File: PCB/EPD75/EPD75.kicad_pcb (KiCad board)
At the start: 2 copper layers, 168 x 110 mm, 73 parts, among them J1 Conn_01x26, J2 Shelly, J3 USB-PROG, J4 BTN1, J5 USB-C-Socket-V, J6 BTN2, J7 USB-C-Socket-V, J8 PWR, P1 2, P10 +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

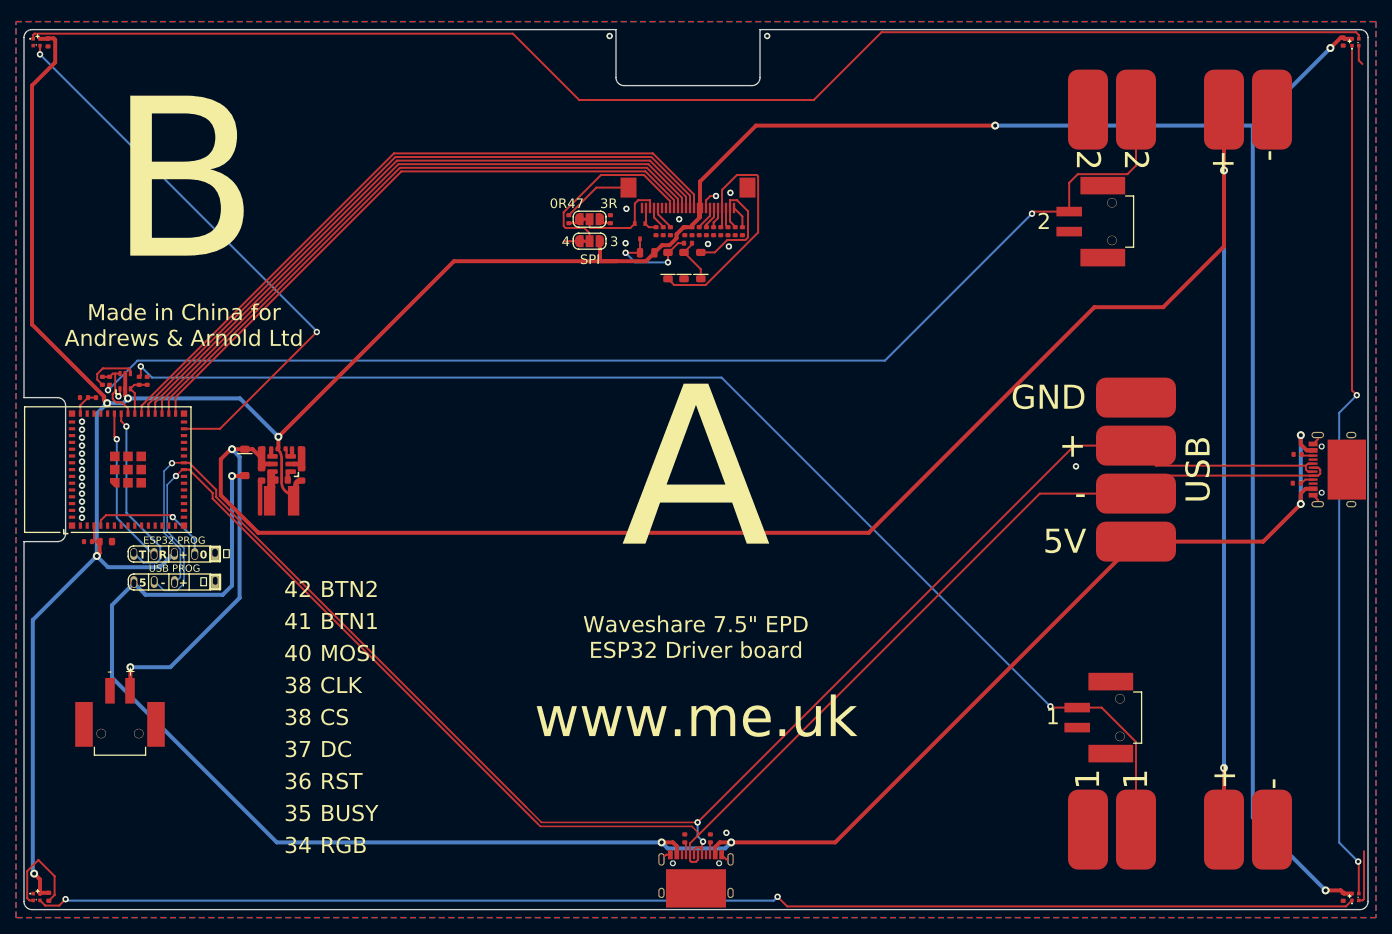
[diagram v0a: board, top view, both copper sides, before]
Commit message: Silk tweak
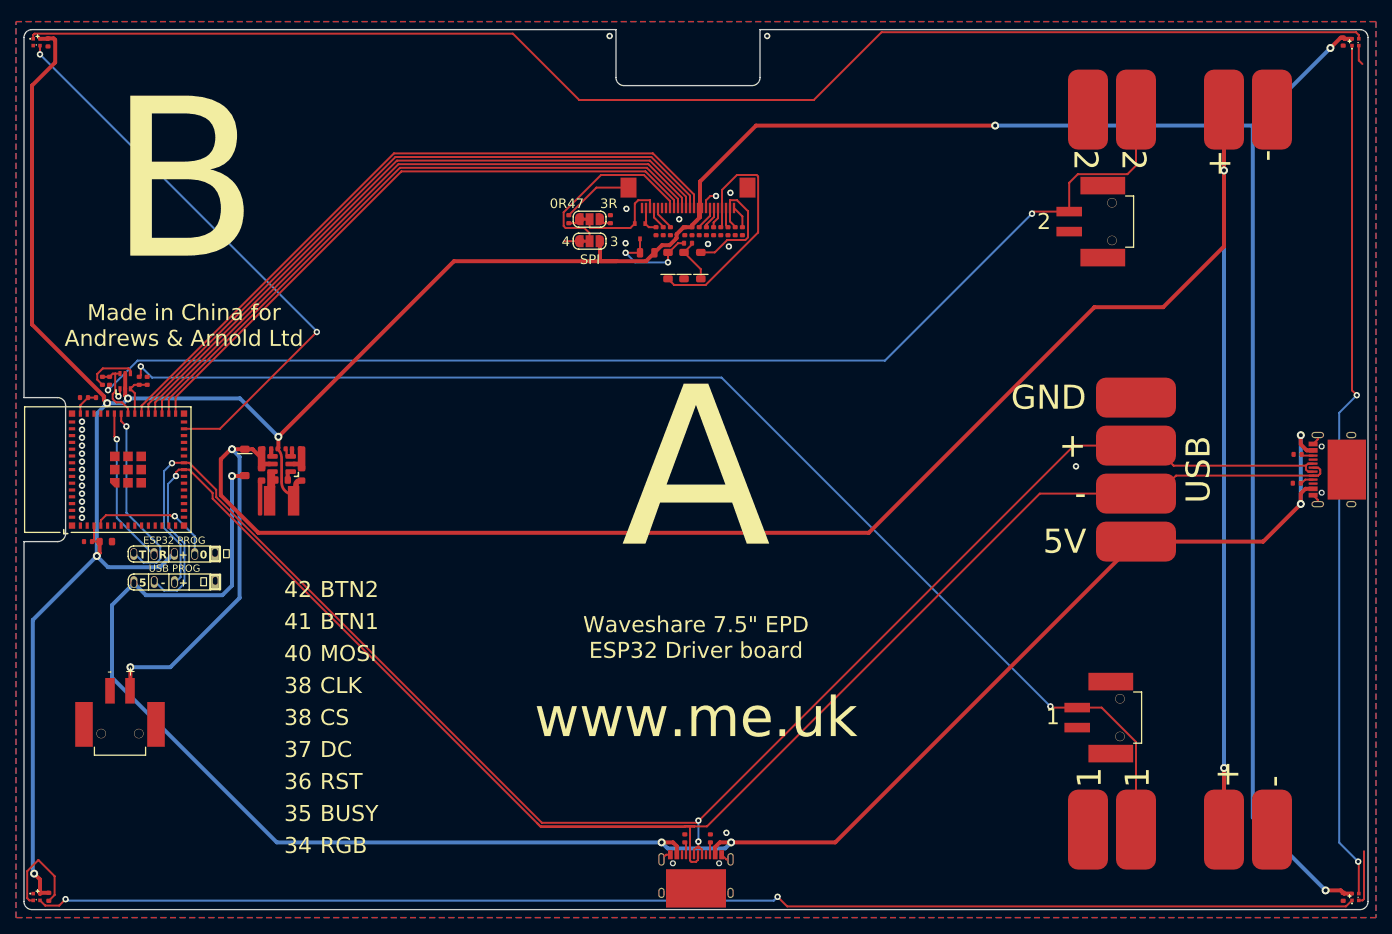
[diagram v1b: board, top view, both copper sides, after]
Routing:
- net D-: track 204.6 -> 224.8 mm
- net D+: track 207.4 -> 204.3 mm

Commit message: Tidy/silk
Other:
- board text added: "${CURRENT_DATE}"

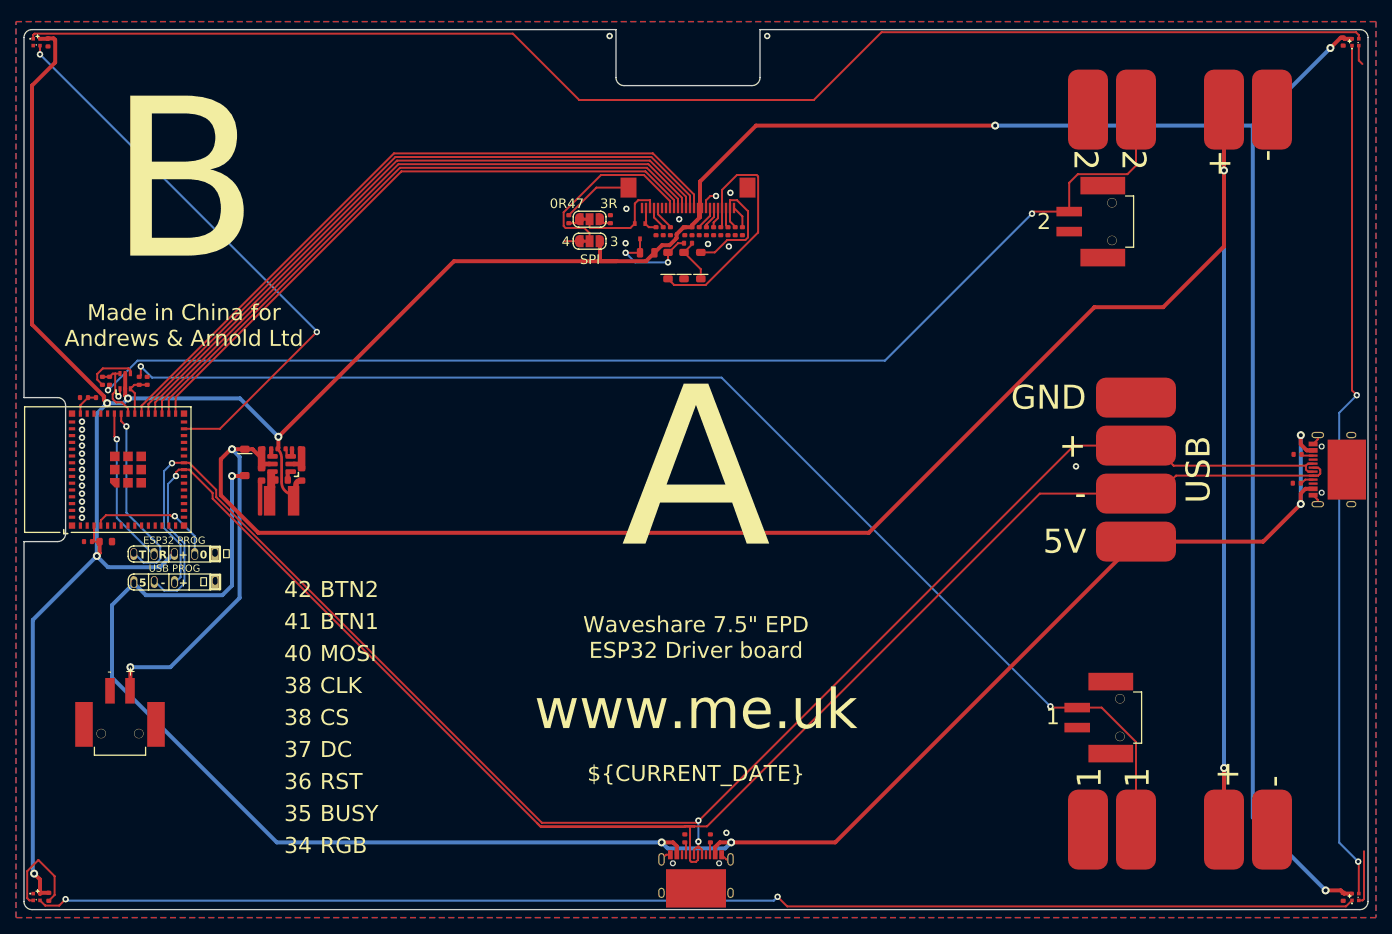
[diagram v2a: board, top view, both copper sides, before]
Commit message: Allow for NFC
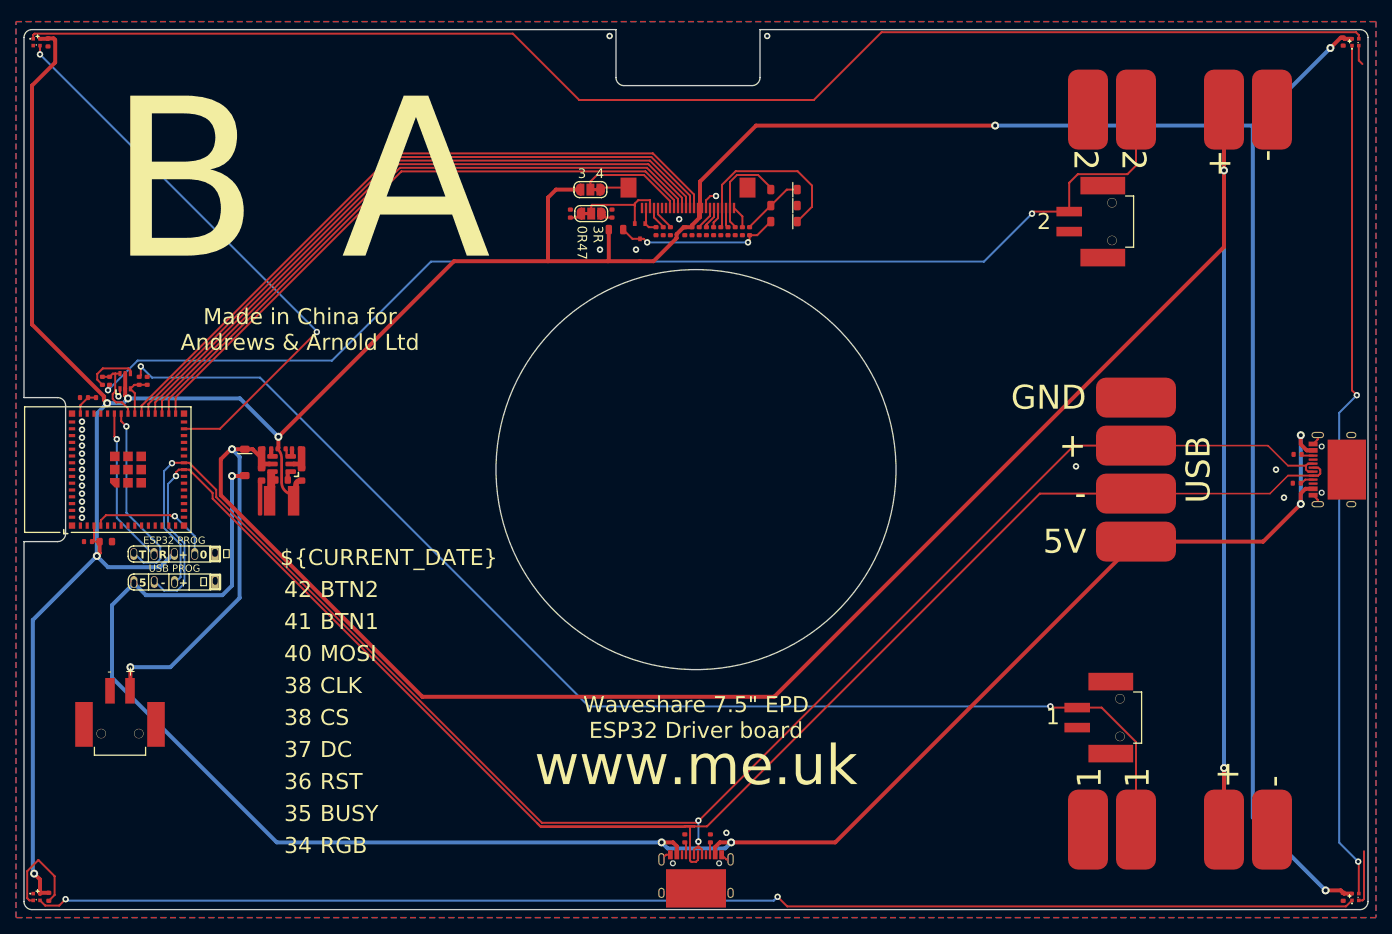
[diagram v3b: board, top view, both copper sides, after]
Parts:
- moved D2 15.5 mm to (111.0, 69.0), turned to 180 degrees
- moved D3 14.6 mm to (111.0, 67.0), turned to 180 degrees
- moved D1 14.1 mm to (111.0, 65.0), turned to 180 degrees
- moved C17 7.84 mm to (106.7, 70.2), turned to 90 degrees
- moved JP1 6.45 mm to (86.8, 65.0), turned to 180 degrees
- moved L1 4.86 mm to (90.0, 70.0), turned to 180 degrees
- moved JP2 0.73 mm to (86.9, 68.0)
- moved R1 0.73 mm to (84.3, 68.0)
- moved R8 0.73 mm to (89.5, 68.0)
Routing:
- net PWR: track 291.4 -> 308.4 mm
- net +3.3V: track 432.1 -> 443.9 mm
- net Net-(J1-Pin_8): track 23.8 -> 13.5 mm
- net Net-(D2-K): track 31.4 -> 23.3 mm
- net Net-(D2-A): track 13.0 -> 20.6 mm
- net GND: track 47.8 -> 40.3 mm, vias 25 -> 24
- net Net-(D1-A): track 16.8 -> 12.0 mm
- net D-: track 224.8 -> 227.5 mm
- net Net-(D1-K): track 5.58 -> 7.88 mm
- net D+: track 204.3 -> 206.5 mm
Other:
- outline, holes or cut-outs redrawn
- board text removed: "SPI"

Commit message: Moved power reg
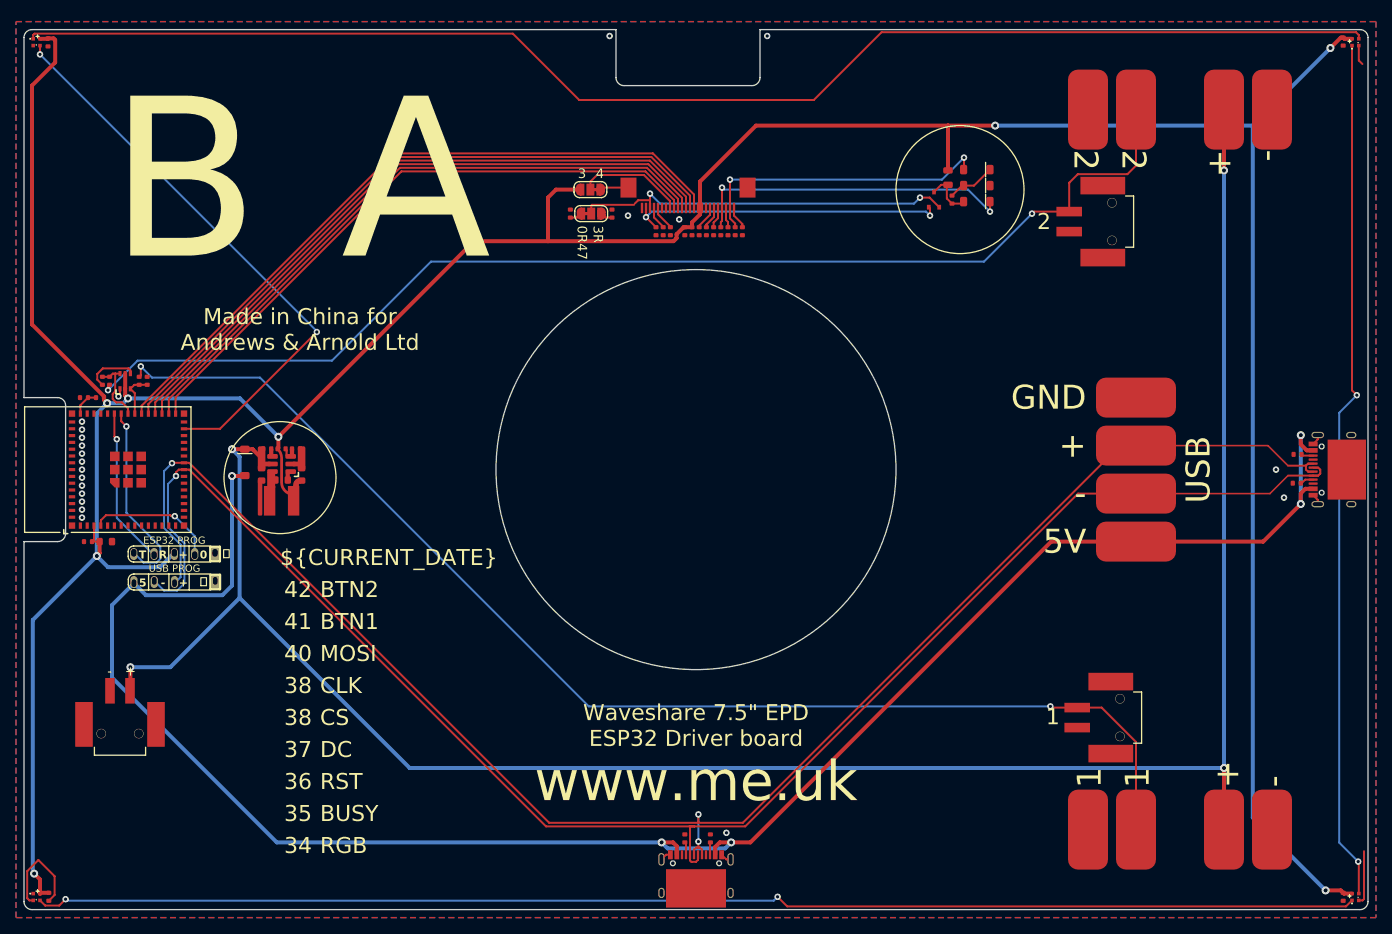
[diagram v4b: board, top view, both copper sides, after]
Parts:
- moved L1 42.0 mm to (131.5, 63.5), turned to 90 degrees
- moved Q1 37.0 mm to (129.8, 66.2), turned to -90 degrees
- moved C17 25.6 mm to (132.0, 66.2)
- moved D1 24.2 mm to (135.1, 62.5)
- moved D2 24.2 mm to (135.1, 66.5)
- moved D3 24.2 mm to (135.1, 64.5)
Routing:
- net PWR: track 308.4 -> 265.1 mm
- net Net-(J1-Pin_3): track 12.1 -> 48.7 mm, vias 0 -> 2
- net Net-(J1-Pin_2): track 3.39 -> 40.0 mm, vias 0 -> 2
- net Net-(D1-A): track 12.0 -> 38.1 mm, vias 0 -> 2
- net D-: track 227.5 -> 207.9 mm
- net Net-(D2-K): track 23.3 -> 41.0 mm, vias 0 -> 2
- net Net-(D2-A): track 20.6 -> 5.79 mm, vias 2 -> 0
- net +3.3V: track 443.9 -> 440.4 mm
- net GND: track 40.3 -> 37.9 mm, vias 24 -> 21
- net Net-(D1-K): track 7.88 -> 5.90 mm
- net D+: track 206.5 -> 205.7 mm
